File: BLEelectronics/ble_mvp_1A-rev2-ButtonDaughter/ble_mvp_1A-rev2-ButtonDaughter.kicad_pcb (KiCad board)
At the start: 2 copper layers, 45.3 x 27.5 mm, 6 parts, among them J1 Nordic_nRF52840_breakout, SW1 SW_Push, SW2 SW_Push, U1 BAT-HLD-001

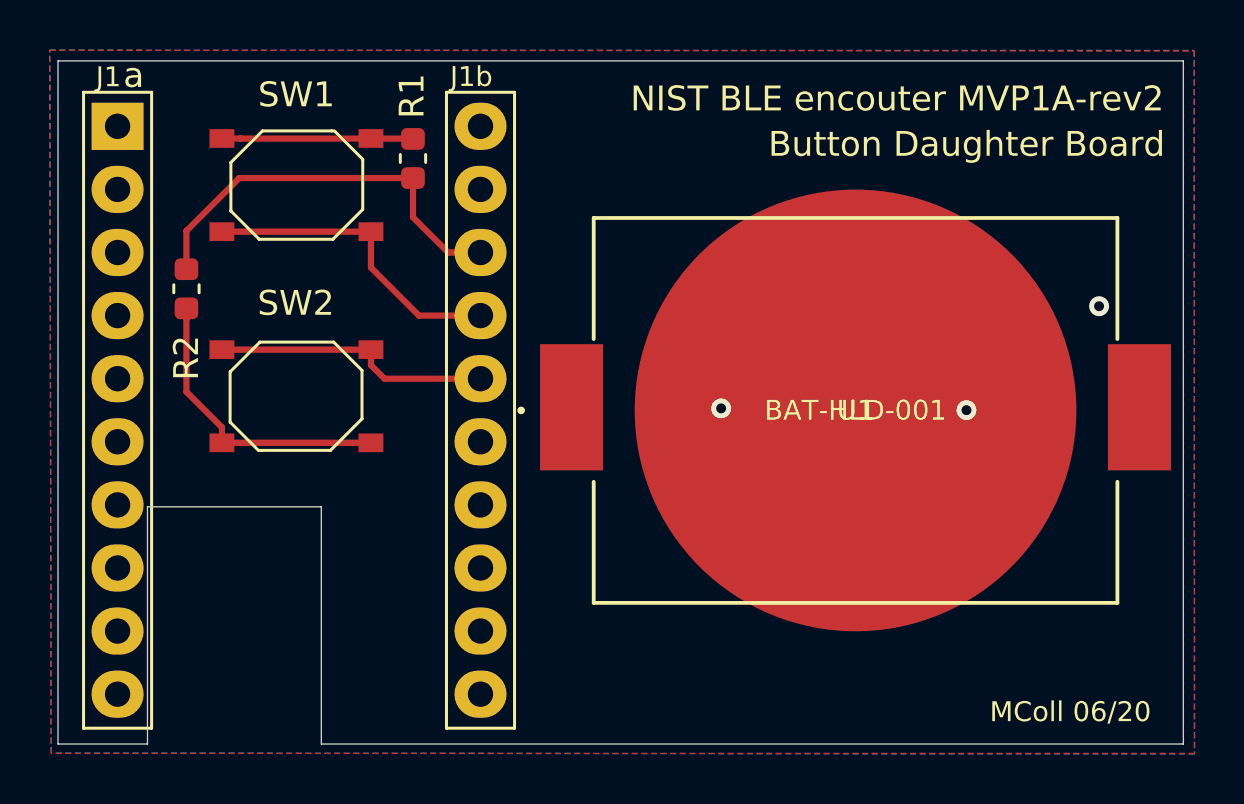
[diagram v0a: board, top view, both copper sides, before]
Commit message: mvp1a-rev2 button daughter board schematic and layout ready for review. ToDo: BOM prep.
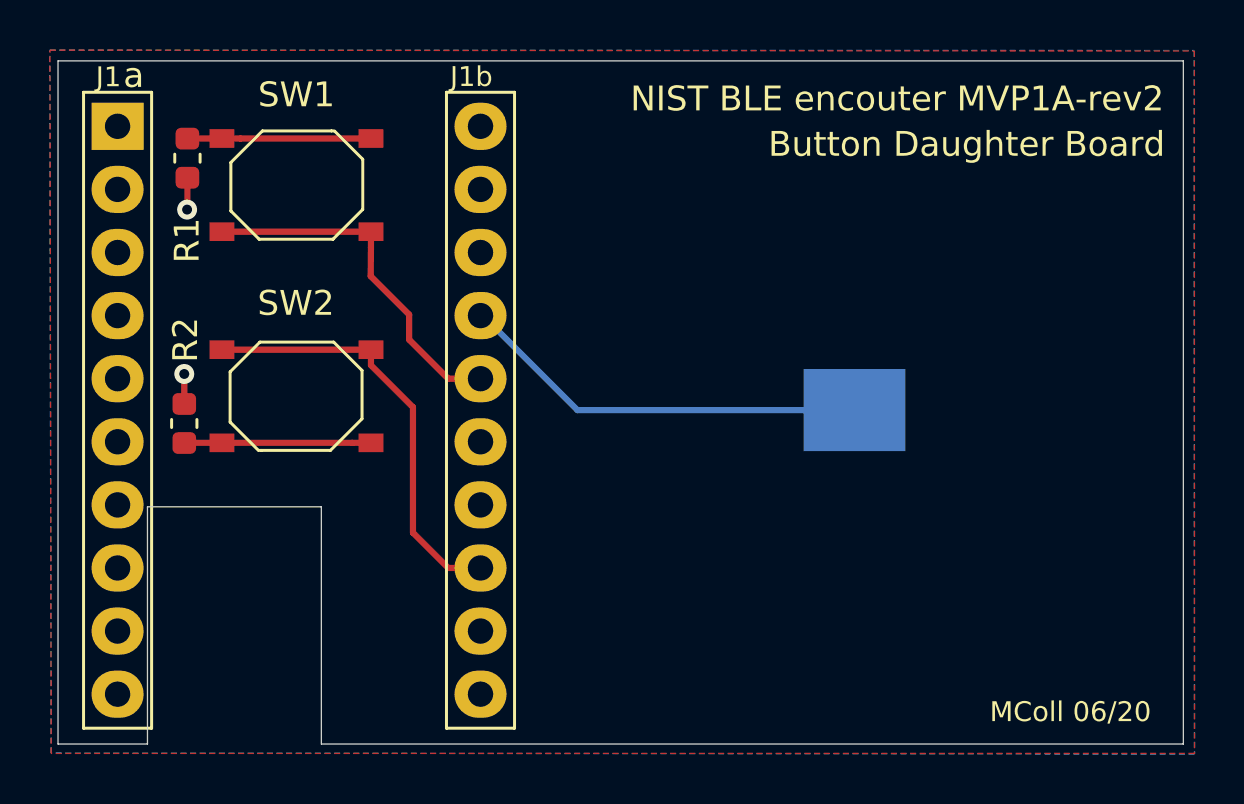
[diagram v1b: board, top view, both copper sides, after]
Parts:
- removed U1: BAT-HLD-001, 0my_footprints:BAT-HLD-001
- added S1: Spring_Finger, 0my_footprints:SpringFingerGeneric, B.Cu at (156.8, 90.6)
- moved R1 9.08 mm to (129.9, 80.4)
- moved R2 5.42 mm to (129.8, 91.1)
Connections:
- J1 pad 13: Net-(J1-Pad13) -> /BigButtonB
- J1 pad 16: /BigButtonB -> /BigButtonA
- J1 pad 17: /BigButtonA -> /BatterySense
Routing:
- net /BatterySense: track 0.00 -> 16.6 mm
- net GND: track 16.4 -> 2.49 mm, vias 1 -> 2
- net /BigButtonB: track 11.3 -> 17.4 mm
- net Net-(R2-Pad1): track 12.0 -> 7.52 mm
- net /BigButtonA: track 12.7 -> 14.5 mm
- net Net-(U1-Pad2): vias 2 -> 0

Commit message: mvp1a-rev2 button daughter board-rev0 ready for production. Also added step files for mvp1a-rev2, Nordic dongle, daughter button board rev0.
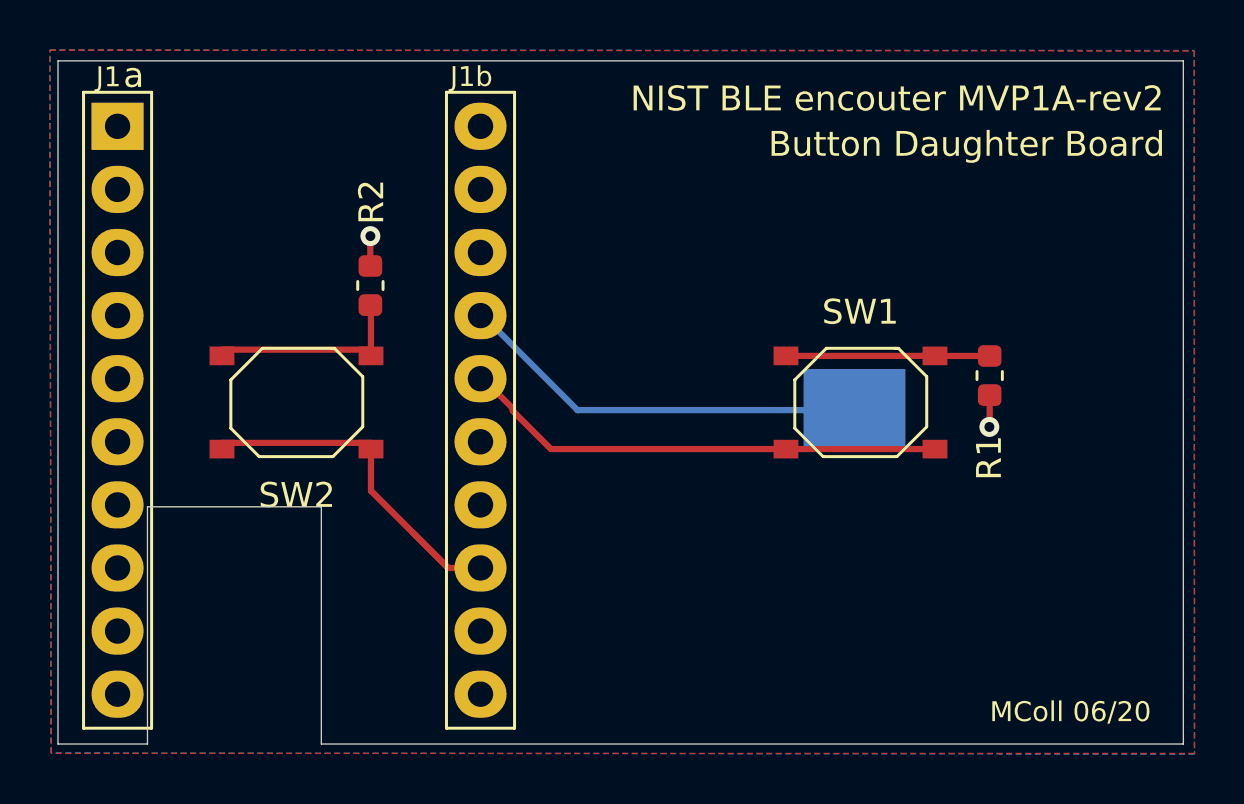
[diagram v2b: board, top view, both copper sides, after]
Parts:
- moved R1 33.5 mm to (162.2, 89.2)
- moved SW1 24.3 mm to (157.0, 90.2)
- moved R2 9.33 mm to (137.3, 85.5)
- moved SW2 0.25 mm to (134.3, 90.2), turned to 180 degrees
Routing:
- net /BigButtonA: track 14.5 -> 19.5 mm
- net /BigButtonB: track 17.4 -> 15.4 mm
- net Net-(R1-Pad1): track 7.39 -> 8.21 mm
- net Net-(R2-Pad1): track 7.52 -> 8.08 mm
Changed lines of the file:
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@@
       (drillshape 0)
       (scaleselection 1)
-      (outputdirectory "gerbers/rev2/"))
+      (outputdirectory "gerbers/ButtonDaught-rev0-formvp1arev2/"))
   )
   (net 0 "")
@@
   )
   (module 0my_footprints:TS-1187A-SMD_button (layer F.Cu)
-    (at 134.2968 90)
+    (at 134.2968 90.25 180)
     (descr http://industrial.panasonic.com/cdbs/www-data/pdf/ATV0000/ATV0000CE5.pdf)
     (tags "SMD SMT SPST EVQPUJ EVQPUA")
@@
       (effects (font (size 1 1) (thickness 0.15)))
     )
-    (pad 1 smd rect (at 3 -1.875 180) (size 1 0.75) (layers F.Cu F.Paste F.Mask)
+    (pad 1 smd rect (at 3 -1.875) (size 1 0.75) (layers F.Cu F.Paste F.Mask)
       (net 16 /BigButtonB))
-    (pad 1 smd rect (at -3 -1.875 180) (size 1 0.75) (layers F.Cu F.Paste F.Mask)
+    (pad 1 smd rect (at -3 -1.875) (size 1 0.75) (layers F.Cu F.Paste F.Mask)
       (net 16 /BigButtonB))
-    (pad 2 smd rect (at -3 1.875 180) (size 1 0.75) (layers F.Cu F.Paste F.Mask)
+    (pad 2 smd rect (at -3 1.875) (size 1 0.75) (layers F.Cu F.Paste F.Mask)
       (net 19 "Net-(R2-Pad1)"))
-    (pad 2 smd rect (at 3 1.875 180) (size 1 0.75) (layers F.Cu F.Paste F.Mask)
+    (pad 2 smd rect (at 3 1.875) (size 1 0.75) (layers F.Cu F.Paste F.Mask)
       (net 19 "Net-(R2-Pad1)"))
     (model ${KISYS3DMOD}/Button_Switch_SMD.3dshapes/Panasonic_EVQPUJ_EVQPUA.wrl
@@
   )
   (module 0my_footprints:TS-1187A-SMD_button (layer F.Cu)
-    (at 134.2968 81.5 180)
+    (at 157 90.25 180)
     (descr http://industrial.panasonic.com/cdbs/www-data/pdf/ATV0000/ATV0000CE5.pdf)
     (tags "SMD SMT SPST EVQPUJ EVQPUA")
@@
   )
   (module Resistor_SMD:R_0603_1608Metric (layer F.Cu)
-    (at 129.7813 91.0971 90)
+    (at 137.2743 85.5432 90)
     (descr "Resistor SMD 0603 (1608 Metric), square (rectangular) end terminal, IPC_7351 nominal, (Body size source: http://www.tortai-tech.com/upload/download/2011102023233369053.pdf), generated with kicad-footprint-generator")
     (tags resistor)
@@
   )
   (module Resistor_SMD:R_0603_1608Metric (layer F.Cu)
-    (at 129.9083 80.4165 270)
+    (at 162.2044 89.1668 270)
     (descr "Resistor SMD 0603 (1608 Metric), square (rectangular) end terminal, IPC_7351 nominal, (Body size source: http://www.tortai-tech.com/upload/download/2011102023233369053.pdf), generated with kicad-footprint-generator")
     (tags resistor)
@@
   (gr_line (start 170 76.5) (end 170 104) (layer Edge.Cuts) (width 0.05))
   (gr_line (start 124.7 76.5) (end 170 76.5) (layer Edge.Cuts) (width 0.05))
-  (via (at 129.7813 89.1032) (size 0.8) (drill 0.4) (layers F.Cu B.Cu) (net 1))
-  (segment (start 129.7813 90.3096) (end 129.7813 89.1032) (width 0.25) (layer F.Cu) (net 1))
-  (via (at 129.8956 82.4865) (size 0.8) (drill 0.4) (layers F.Cu B.Cu) (net 1))
-  (segment (start 129.9083 81.204) (end 129.9083 82.4738) (width 0.25) (layer F.Cu) (net 1))
-  (segment (start 129.9083 82.4738) (end 129.8956 82.4865) (width 0.25) (layer F.Cu) (net 1))
+  (via (at 137.2743 83.5533) (size 0.8) (drill 0.4) (layers F.Cu B.Cu) (net 1))
+  (via (at 162.1917 91.2368) (size 0.8) (drill 0.4) (layers F.Cu B.Cu) (net 1))
+  (segment (start 162.2044 89.9543) (end 162.2044 91.2241) (width 0.25) (layer F.Cu) (net 1))
+  (segment (start 162.2044 91.2241) (end 162.1917 91.2368) (width 0.25) (layer F.Cu) (net 1))
+  (segment (start 137.2743 84.7557) (end 137.2743 83.5533) (width 0.25) (layer F.Cu) (net 1))
   (segment (start 142.0068 94.3737) (end 141.9068 94.3737) (width 0.25) (layer B.Cu) (net 4))
   (segment (start 126.7968 89.94394) (end 126.8968 89.94394) (width 0.25) (layer F.Cu) (net 7))
   (segment (start 126.8968 91.8337) (end 127.518221 92.455121) (width 0.25) (layer F.Cu) (net 15))
-  (segment (start 131.2968 88.125) (end 137.2968 88.125) (width 0.25) (layer F.Cu) (net 16))
-  (segment (start 137.2968 88.75) (end 137.2968 88.125) (width 0.25) (layer F.Cu) (net 16))
-  (segment (start 138.9888 90.442) (end 137.2968 88.75) (width 0.25) (layer F.Cu) (net 16))
-  (segment (start 138.9888 95.4957) (end 138.9888 90.442) (width 0.25) (layer F.Cu) (net 16))
+  (segment (start 131.2968 88.125) (end 137.2968 88.125) (width 0.25) (layer F.Cu) (net 19))
+  (segment (start 140.4068 96.9137) (end 138.9888 95.4957) (width 0.25) (layer F.Cu) (net 16))
+  (segment (start 160 92.125) (end 154 92.125) (width 0.25) (layer F.Cu) (net 17))
+  (segment (start 141.8068 89.2937) (end 141.7068 89.2937) (width 0.25) (layer F.Cu) (net 17))
+  (segment (start 143.0068 90.4937) (end 141.8068 89.2937) (width 0.25) (layer F.Cu) (net 17))
+  (segment (start 144.5381 92.125) (end 143.0068 90.5937) (width 0.25) (layer F.Cu) (net 17))
+  (segment (start 143.0068 90.5937) (end 143.0068 90.4937) (width 0.25) (layer F.Cu) (net 17))
+  (segment (start 154 92.125) (end 144.5381 92.125) (width 0.25) (layer F.Cu) (net 17))
+  (segment (start 162.2084 88.3753) (end 162.2044 88.3793) (width 0.25) (layer F.Cu) (net 18))
+  (segment (start 160.0043 88.3793) (end 160 88.375) (width 0.25) (layer F.Cu) (net 18))
+  (segment (start 162.2044 88.3793) (end 160.0043 88.3793) (width 0.25) (layer F.Cu) (net 18))
+  (segment (start 154 88.375) (end 160 88.375) (width 0.25) (layer F.Cu) (net 18))
+  (segment (start 136.5468 91.875) (end 131.2968 91.875) (width 0.25) (layer F.Cu) (net 16))
+  (segment (start 137.2968 91.875) (end 136.5468 91.875) (width 0.25) (layer F.Cu) (net 16))
+  (segment (start 137.2968 92.75) (end 137.2968 92.125) (width 0.25) (layer F.Cu) (net 16))
+  (segment (start 137.2968 93.8037) (end 137.2968 92.75) (width 0.25) (layer F.Cu) (net 16))
+  (segment (start 140.4068 96.9137) (end 137.2968 93.8037) (width 0.25) (layer F.Cu) (net 16))
   (segment (start 141.7068 96.9137) (end 140.4068 96.9137) (width 0.25) (layer F.Cu) (net 16))
-  (segment (start 140.4068 96.9137) (end 138.9888 95.4957) (width 0.25) (layer F.Cu) (net 16))
-  (segment (start 131.2968 83.375) (end 137.2968 83.375) (width 0.25) (layer F.Cu) (net 17))
-  (segment (start 137.2968 84) (end 137.2968 83.375) (width 0.25) (layer F.Cu) (net 17))
-  (segment (start 141.7068 89.2937) (end 140.4068 89.2937) (width 0.25) (layer F.Cu) (net 17))
-  (segment (start 138.8342 86.7134) (end 137.287 85.1662) (width 0.25) (layer F.Cu) (net 17))
-  (segment (start 138.8342 87.7211) (end 138.8342 86.7134) (width 0.25) (layer F.Cu) (net 17))
-  (segment (start 140.4068 89.2937) (end 138.8342 87.7211) (width 0.25) (layer F.Cu) (net 17))
-  (segment (start 137.287 85.1662) (end 137.2968 84) (width 0.25) (layer F.Cu) (net 17))
-  (segment (start 132.0468 79.625) (end 137.2968 79.625) (width 0.25) (layer F.Cu) (net 18))
-  (segment (start 131.2968 79.625) (end 132.0468 79.625) (width 0.25) (layer F.Cu) (net 18))
-  (segment (start 129.9123 79.625) (end 129.9083 79.629) (width 0.25) (layer F.Cu) (net 18))
-  (segment (start 131.2968 79.625) (end 129.9123 79.625) (width 0.25) (layer F.Cu) (net 18))
-  (segment (start 136.5468 91.875) (end 131.2968 91.875) (width 0.25) (layer F.Cu) (net 19))
-  (segment (start 137.2968 91.875) (end 136.5468 91.875) (width 0.25) (layer F.Cu) (net 19))
-  (segment (start 129.7909 91.875) (end 129.7813 91.8846) (width 0.25) (layer F.Cu) (net 19))
-  (segment (start 131.2968 91.875) (end 129.7909 91.875) (width 0.25) (layer F.Cu) (net 19))
+  (segment (start 137.2899 86.3463) (end 137.2743 86.3307) (width 0.25) (layer F.Cu) (net 19))
+  (segment (start 137.2968 86.3532) (end 137.2743 86.3307) (width 0.25) (layer F.Cu) (net 19))
+  (segment (start 137.2968 88.375) (end 137.2968 86.3532) (width 0.25) (layer F.Cu) (net 19))
   (segment (start 141.8068 86.7537) (end 141.7068 86.7537) (width 0.25) (layer B.Cu) (net 20))
   (segment (start 145.6131 90.56) (end 141.8068 86.7537) (width 0.25) (layer B.Cu) (net 20))
